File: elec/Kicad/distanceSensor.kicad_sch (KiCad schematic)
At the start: 0 parts

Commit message: sa progresse. Battery management fini + humidity/temp sensor + bouton
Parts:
- added U5: VL53L0CXV0DH1, Sensor_Distance:ST_VL53L1x, symbol Sensor_Distance:VL53L0CXV0DH1
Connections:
- new net: U5.12 (GND), U5.3 (GND), U5.4 (GND), U5.6 (GND)
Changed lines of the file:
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@@
 	(generator_version "8.0")
 	(paper "A4")
+	(symbol
+		(lib_id "Sensor_Distance:VL53L0CXV0DH1")
+		(at 74.93 76.2 0)
+		(unit 1)
+		(exclude_from_sim no)
+		(in_bom yes)
+		(on_board yes)
+		(dnp no)
+		(fields_autoplaced yes)
+		(property "Reference" "U5"
+			(at 83.82 74.9299 0)
+			(effects
+				(font
+					(size 1.27 1.27)
+				)
+				(justify left)
+			)
+		)
+		(property "Value" "VL53L0CXV0DH1"
+			(at 83.82 77.4699 0)
+			(effects
+				(font
+					(size 1.27 1.27)
+				)
+				(justify left)
+			)
+		)
+		(property "Footprint" "Sensor_Distance:ST_VL53L1x"
+			(at 92.075 90.17 0)
+			(effects
+				(font
+					(size 1.27 1.27)
+				)
+				(hide yes)
+			)
+		)
+		(property "Datasheet" "https://www.st.com/resource/en/datasheet/vl53l0x.pdf"
+			(at 77.47 76.2 0)
+			(effects
+				(font
+					(size 1.27 1.27)
+				)
+				(hide yes)
+			)
+		)
+		(property "Description" "2m distance ranging ToF sensor, Optical LGA12"
+			(at 74.93 76.2 0)
+			(effects
+				(font
+					(size 1.27 1.27)
+				)
+				(hide yes)
+			)
+		)
+		(pin "12"
+		)
+		(pin "10"
+		)
+		(pin "5"
+		)
+		(pin "8"
+		)
+		(pin "1"
+		)
+		(pin "11"
+		)
+		(pin "6"
+		)
+		(pin "7"
+		)
+		(pin "3"
+		)
+		(pin "2"
+		)
+		(pin "9"
+		)
+		(pin "4"
+		)
+		(instances
+			(project ""
+				(path "/a1545928-1195-40b9-b3c4-78f837012afb/5f7b9d88-eb12-47e8-8ae8-265c4903ec29"
+					(reference "U5")
+					(unit 1)
+				)
+			)
+		)
+	)
 )

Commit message: ta grand-maman
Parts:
- added C10: 4.7uF, symbol Device:C
- added C11: 100nF, symbol Device:C
- added C12, C13: 10uF, symbol Device:C
- added U6: MIC5219-2.8YM5, Package_TO_SOT_SMD:SOT-23-5, symbol Regulator_Linear:MIC5219-2.8YM5
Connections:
- net +3.3V: now reaches U5.1 (AVDDVCSEL)
- net +3.3V: now also U5.11 (AVDD), C10.1, C11.1
- net GND: now reaches U5.12 (GND), U5.3 (GND), U5.4 (GND), U5.6 (GND)
- net GND: now also U5.2 (AVSSVCSEL), C10.2, C11.2, C12.2, C13.2, U6.2 (GND)
- new net: C12.1, U6.1 (IN), U6.3 (EN)
- new net: C13.1, U6.5 (OUT)
- no-connect marks 0 -> 1

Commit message: merci charles de m'aider a nous aider
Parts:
- added C15: 1uF, symbol Device:C
- added J4: Conn_01x05, symbol Connector_Generic:Conn_01x05
- added JP1: SolderJumper_2_Open, symbol Jumper:SolderJumper_2_Open
- added Q2, Q3: BSS138, Package_TO_SOT_SMD:SOT-23, symbol Transistor_FET:BSS138
- added R15, R16: 10K, symbol Device:R
- added R17: 1K, symbol Device:R
- C12: value 10uF -> 100nF
- C13: value 10uF -> 1uF
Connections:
- net +3.3V: now also C12.1, U6.1 (IN), U6.3 (EN), C15.1, J4.1 (Pin_1); no longer C10.1, C11.1, U5.1 (AVDDVCSEL), U5.11 (AVDD)
- net GND: now also C15.2, J4.5 (Pin_5)
- net SCL_2V8: now reaches U5.10 (SCL)
- net SCL_2V8: now also Q3.2 (S), R16.2
- net at U5.5 (XSHUT): now also JP1.1 (A), R17.2
- net SDA_2V8: now reaches U5.9 (SDA)
- net SDA_2V8: now also Q2.2 (S), R15.2
- net +2V8: now reaches C13.1, U6.5 (OUT)
- net +2V8: now also C10.1, C11.1, U5.1 (AVDDVCSEL), U5.11 (AVDD), JP1.2 (B), Q2.1 (G), Q3.1 (G), R15.1, R16.1
- new net I2C1_SCL: J4.2 (Pin_2), Q3.3 (D)
- new net I2C1_SDA: J4.3 (Pin_3), Q2.3 (D)
- new net XSHUT: J4.4 (Pin_4), R17.1
- no-connect marks 1 -> 2
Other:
- note added: "Ceci est un petit PCB on veux pouvoir le retirer et le remettre avec un header"
- note added: "GPIO1 est une sortie qui permet de trigg des interrupt ex: distance aillant atteint un seuil prédéfini options: 1. soit on le connecte pour avoir des notifs 2. on le connect pas (présentement pas connecté)"
- note added: "Magouille pour transformer la logique SDA/SCL qui est de 3.3V a une logique SDA/SCL de 2.8V Trust it should work (In JULIEN we Trust)"
- note added: "XSHUT = peremet de désactiver le capteur en mettant cette broche a LOW. Il ne consommera pas bcp d'énergie a ce momment là options: 1. soit on le met a high (2.8V) 2. on le connecte au MCU et qu'on le met a high quand on veux l'utiliser (présentement connecté)"
- moved on the sheet: C10, C11, C12, C13, U5, U6

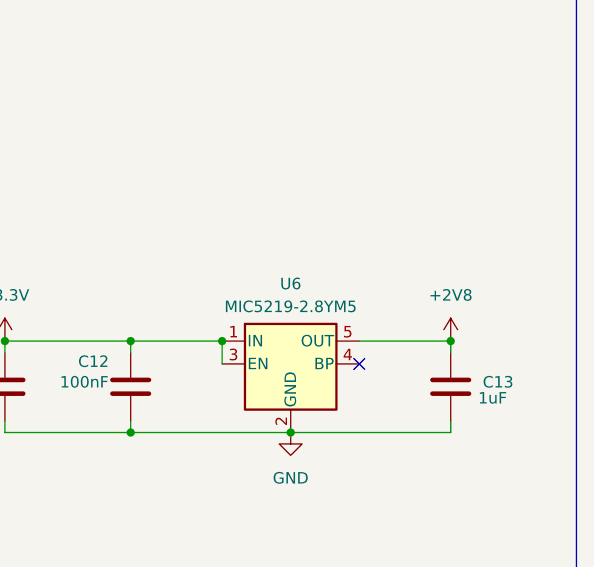
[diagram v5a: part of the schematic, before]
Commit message: push pour charles (début de l'ajout diviseur tension pour la batterie)
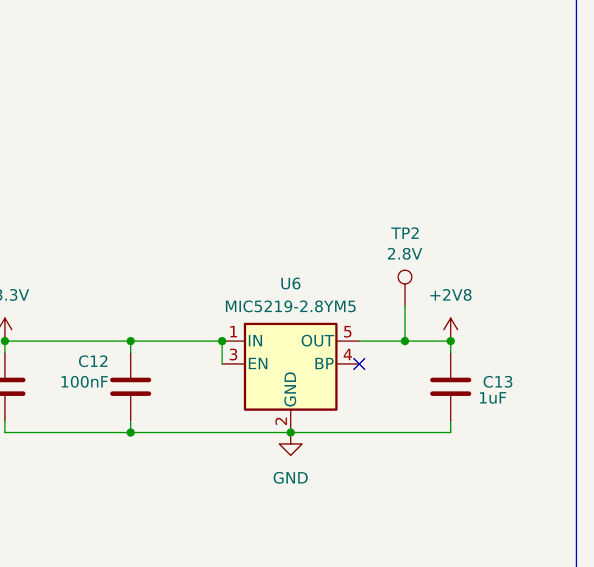
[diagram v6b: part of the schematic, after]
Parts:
- added TP2: 2.8V, symbol Connector:TestPoint
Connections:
- net +2V8: now also TP2.1
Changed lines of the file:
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@@
+	)
+	(junction
+		(at 223.52 82.55)
+		(diameter 0)
+		(color 0 0 0 0)
 	)
 	(junction
@@
 	(wire
 		(pts
+			(xy 223.52 82.55) (xy 228.6 82.55)
+		)
+		(stroke
+			(width 0)
+			(type default)
+		)
+	)
+	(wire
+		(pts
 			(xy 228.6 91.44) (xy 228.6 92.71)
 		)
@@
 	(wire
 		(pts
+			(xy 223.52 78.74) (xy 223.52 82.55)
+		)
+		(stroke
+			(width 0)
+			(type default)
+		)
+	)
+	(wire
+		(pts
 			(xy 69.85 67.31) (xy 82.55 67.31)
 		)
@@
 	(wire
 		(pts
-			(xy 218.44 82.55) (xy 228.6 82.55)
+			(xy 218.44 82.55) (xy 223.52 82.55)
 		)
 		(stroke
@@
 					(unit 1)
 				)
+			)
+		)
+	)
+	(symbol
+		(lib_id "Connector:TestPoint")
+		(at 223.52 78.74 0)
+		(unit 1)
+		(exclude_from_sim no)
+		(in_bom yes)
+		(on_board yes)
+		(dnp no)
+		(property "Reference" "TP2"
+			(at 221.996 70.612 0)
+			(effects
+				(font
+					(size 1.27 1.27)
+				)
+				(justify left)
+			)
+		)
+		(property "Value" "2.8V"
+			(at 221.488 72.898 0)
+			(effects
+				(font
+					(size 1.27 1.27)
+				)
+				(justify left)
+			)
+		)
+		(property "Footprint" ""
+			(at 228.6 78.74 0)
+			(effects
+				(font
+					(size 1.27 1.27)
+				)
+				(hide yes)
+			)
+		)
+		(property "Datasheet" "~"
+			(at 228.6 78.74 0)
+			(effects
+				(font
+					(size 1.27 1.27)
+				)
+				(hide yes)
+			)
+		)
+		(property "Description" "test point"
+			(at 223.52 78.74 0)
+			(effects
+				(font
+					(size 1.27 1.27)
+				)
+				(hide yes)
+			)
+		)
+		(pin "1"
+		)
+		(instances
+			(project ""
+				(path "/a1545928-1195-40b9-b3c4-78f837012afb/5f7b9d88-eb12-47e8-8ae8-265c4903ec29"
+					(reference "TP2")
+					(unit 1)
+				)

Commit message: va falloir faire le PCB soon
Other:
- note added: "I2C address=0x52"
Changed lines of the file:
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@@
+		)
+	)
+	(text "I2C address=0x52\n"
+		(exclude_from_sim no)
+		(at 128.016 61.468 0)
+		(effects
+			(font
+				(size 1.27 1.27)
+			)
 		)
 	)
